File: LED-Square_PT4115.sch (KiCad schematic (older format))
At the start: 21 parts, among them P1 IN, P2 OUT, U1 PT4115-SOT89-5

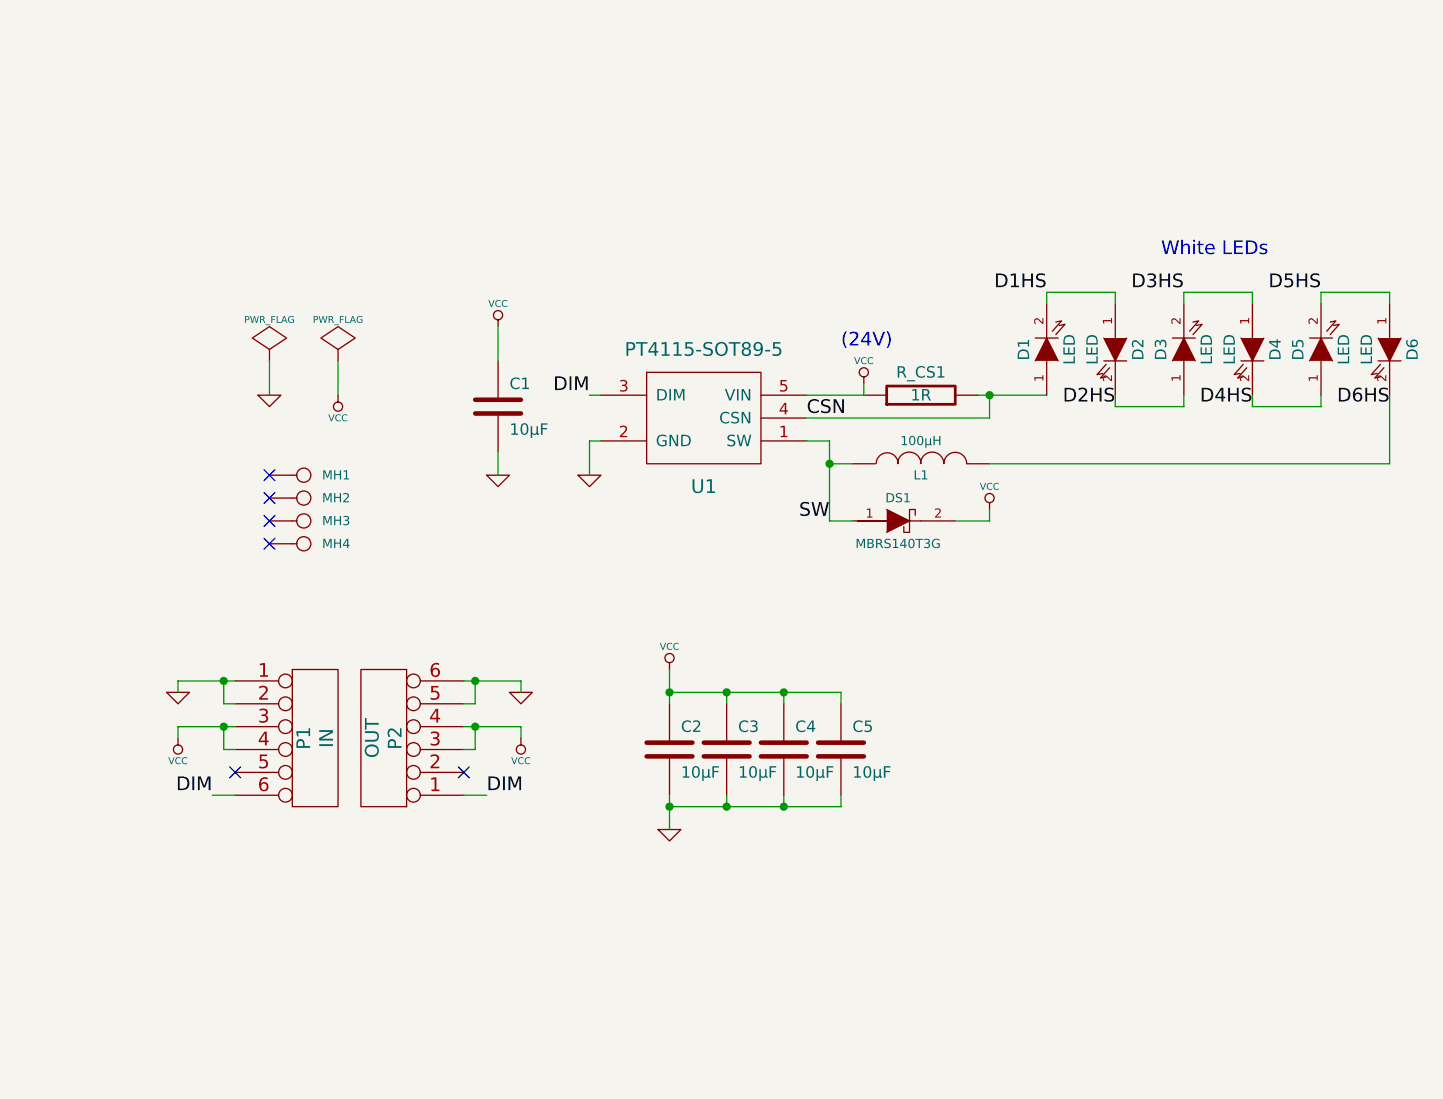
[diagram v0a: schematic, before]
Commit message: Added soft-start capacitor(s) - optional.
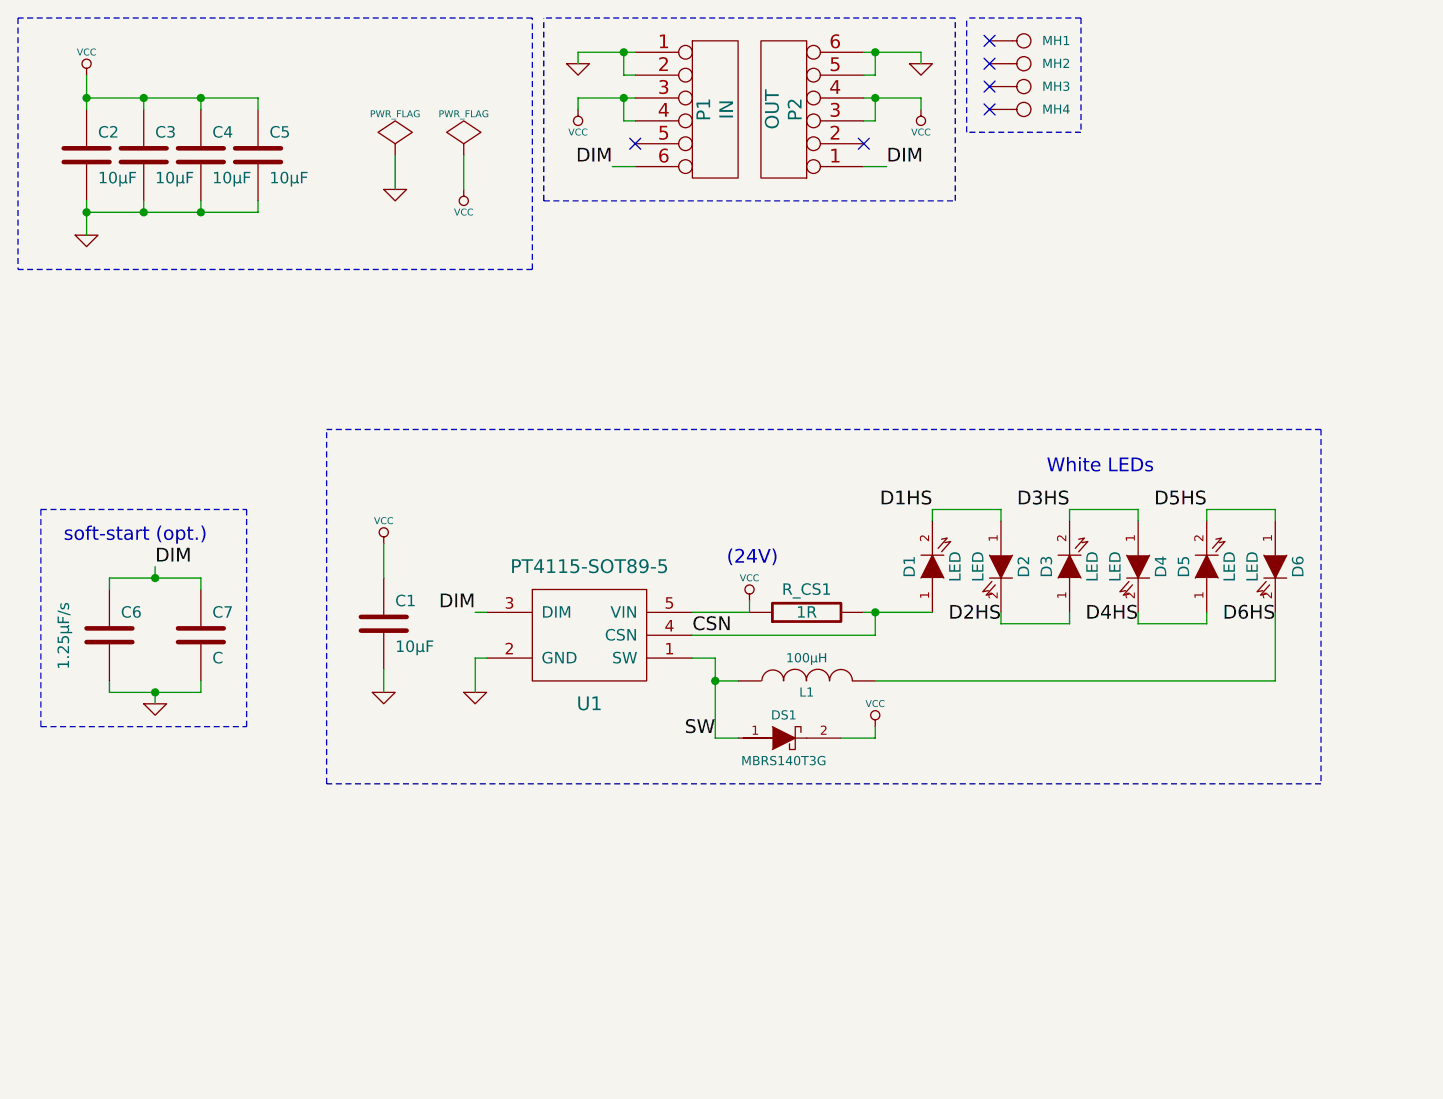
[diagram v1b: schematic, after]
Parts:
- added C6: 1.25µF/s, symbol C
- added C7: C, symbol C
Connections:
- net DIM: now also C6.1, C7.1
- net GND: now also C6.2, C7.2
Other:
- note added: "soft-start (opt.)"
- moved on the sheet: C1, C2, C3, C4, C5, D1, D2, D3, D4, D5, D6, DS1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

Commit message: Soft-start: replaced C7 with R1 (1M bleed resistor) for remaining C6.
R1 is not strictly necessary, but it speeds up discharging C6 a lot.
Without R1 it takes some time, maybe minutes, until soft-start
works again.
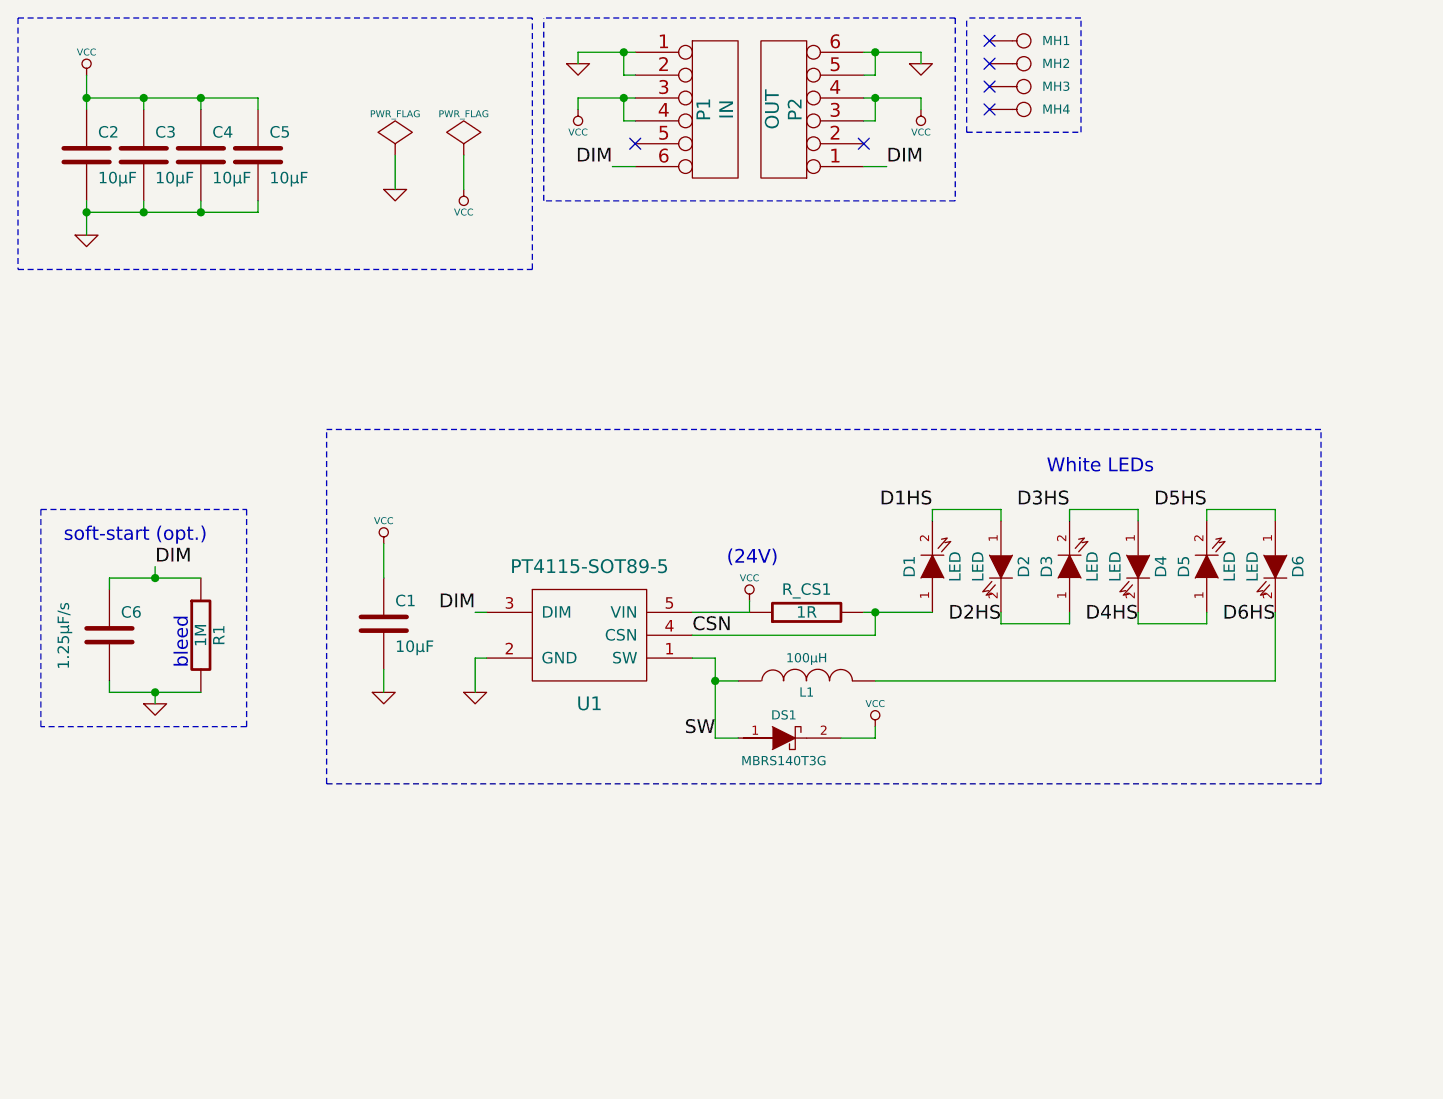
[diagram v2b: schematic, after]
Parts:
- removed C7: C, symbol C
- added R1: 1M, symbol R
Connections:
- net DIM: now also R1.1
- net GND: now also R1.2
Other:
- note added: "bleed"
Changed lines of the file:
@@
-EESchema Schematic File Version 2  date Sat 27 Oct 2012 06:55:14 PM CEST
+EESchema Schematic File Version 2  date Sun 11 Nov 2012 12:08:53 AM CET
 LIBS:my_parts
 LIBS:power
@@
 Sheet 1 1
 Title "LED-Square PT4115"
-Date "27 oct 2012"
+Date "10 nov 2012"
 Rev "0.10"
 Comp "2012 - blog.spitzenpfeil.org"
@@
 Comment4 ""
 $EndDescr
+Text Notes 1300 3400 1    60   ~ 0
+bleed
+Connection ~ 1150 3000
+Wire Wire Line
+	1150 2950 1150 3000
+Wire Wire Line
+	1350 3500 950  3500
+Wire Wire Line
+	1350 3000 950  3000
+Wire Notes Line
+	1550 3650 1550 2700
+Wire Notes Line
+	1550 3650 650  3650
+Wire Notes Line
+	650  3650 650  2700
+Wire Notes Line
+	550  550  550  1650
+Wire Notes Line
+	4700 1050 4700 550
+Wire Notes Line
+	4700 1050 5200 1050
+Wire Notes Line
+	5200 1050 5200 550
+Wire Notes Line
+	5200 550  4700 550
+Wire Notes Line
+	4650 550  2850 550
+Wire Notes Line
+	4650 550  4650 1350
+Wire Notes Line
+	4650 1350 2850 1350
+Wire Notes Line
+	2850 1350 2850 550
+Connection ~ 850  900
+Wire Wire Line
+	850  800  850  950
+Connection ~ 1100 1400
+Wire Wire Line
+	1100 1350 1100 1400
+Wire Wire Line
+	1600 1350 1600 1400
+Wire Wire Line
+	1600 1400 850  1400
+Connection ~ 1350 900
+Wire Wire Line
+	1350 950  1350 900
+Connection ~ 4300 700
+Wire Wire Line
+	4300 700  4300 800
+Wire Wire Line
+	4300 800  4250 800
+Connection ~ 4300 900
+Wire Wire Line
+	4300 900  4300 1000
+Wire Wire Line
+	4300 1000 4250 1000
+Wire Wire Line
+	4250 1200 4350 1200
+Wire Wire Line
+	3150 1200 3250 1200
+Wire Wire Line
+	3250 1000 3200 1000
+Connection ~ 3200 900
+Wire Wire Line
+	3200 1000 3200 900
+Connection ~ 3200 700
+Wire Wire Line
+	3200 700  3200 800
+Wire Wire Line
+	3200 800  3250 800
+Wire Wire Line
+	2500 1150 2500 1300
+Connection ~ 3600 3450
+Wire Wire Line
+	3700 3700 3600 3700
+Wire Wire Line
+	3600 3700 3600 3350
+Wire Wire Line
+	6050 3150 6050 3450
+Wire Wire Line
+	6050 3450 4300 3450
+Connection ~ 4300 3150
+Wire Wire Line
+	4550 3150 4250 3150
+Wire Wire Line
+	2150 2850 2150 3000
+Wire Wire Line
+	3750 3100 3750 3150
+Wire Wire Line
+	3750 3150 3500 3150
+Wire Wire Line
+	6050 2750 6050 2700
+Wire Wire Line
+	6050 2700 5750 2700
+Wire Wire Line
+	5750 2700 5750 2750
+Wire Wire Line
+	5450 2750 5450 2700
+Wire Wire Line
+	5450 2700 5150 2700
+Wire Wire Line
+	5150 2700 5150 2750
+Wire Wire Line
+	4850 2750 4850 2700
+Wire Wire Line
+	4850 2700 4550 2700
+Wire Wire Line
+	4550 2700 4550 2750
+Wire Wire Line
+	4850 3150 4850 3200
+Wire Wire Line
+	4850 3200 5150 3200
+Wire Wire Line
+	5150 3200 5150 3150
+Wire Wire Line
+	5450 3150 5450 3200
+Wire Wire Line
+	5450 3200 5750 3200
+Wire Wire Line
+	5750 3200 5750 3150
+Wire Wire Line
+	2600 3350 2550 3350
+Wire Wire Line
+	2550 3350 2550 3500
+Wire Wire Line
+	3500 3250 4300 3250
+Wire Wire Line
+	4300 3250 4300 3150
+Wire Wire Line
+	2150 3400 2150 3500
+Wire Wire Line
+	3600 3350 3500 3350
+Wire Wire Line
+	3600 3450 3700 3450
+Wire Wire Line
+	4150 3700 4300 3700
+Wire Wire Line
+	4300 3700 4300 3650
+Wire Wire Line
+	2200 1150 2200 1300
+Wire Wire Line
+	3000 750  3000 700
+Wire Wire Line
+	3000 700  3250 700
+Wire Wire Line
+	3000 950  3000 900
+Wire Wire Line
+	3000 900  3250 900
+Wire Wire Line
+	2550 3150 2600 3150
+Wire Wire Line
+	4250 900  4500 900
+Wire Wire Line
+	4500 900  4500 950
+Wire Wire Line
+	4250 700  4500 700
+Wire Wire Line
+	4500 700  4500 750
+Wire Wire Line
+	850  900  1600 900
+Wire Wire Line
+	1600 900  1600 950
+Wire Wire Line
+	1100 950  1100 900
+Connection ~ 1100 900
+Wire Wire Line
+	1350 1350 1350 1400
+Connection ~ 1350 1400
+Wire Wire Line
+	850  1500 850  1350
+Connection ~ 850  1400
+Wire Notes Line
+	550  550  2800 550
+Wire Notes Line
+	550  1650 2800 1650
+Wire Notes Line
+	2800 1650 2800 550
+Wire Notes Line
+	1900 3900 1900 2350
+Wire Notes Line
+	1900 3900 6250 3900
+Wire Notes Line
+	6250 3900 6250 2350
+Wire Notes Line
+	6250 2350 1900 2350
+Wire Wire Line
+	950  3000 950  3050
+Wire Wire Line
+	950  3500 950  3450
 Wire Notes Line
 	650  2700 1550 2700
 Wire Wire Line
-	1150 3500 1150 3550
-Connection ~ 1150 3000
-Wire Wire Line
-	1350 3450 1350 3500
-Wire Wire Line
-	1350 3500 950  3500
-Wire Wire Line
-	950  3500 950  3450
-Wire Wire Line
-	950  3050 950  3000
-Wire Notes Line
-	6250 2350 1900 2350
-Wire Notes Line
-	6250 2350 6250 3900
-Wire Notes Line
-	6250 3900 1900 3900
-Wire Notes Line
-	1900 3900 1900 2350
-Wire Notes Line
-	2800 1650 2800 550
-Wire Notes Line
-	2800 1650 550  1650
-Wire Notes Line
-	2800 550  550  550
-Connection ~ 850  1400
-Wire Wire Line
-	850  1500 850  1350
-Connection ~ 1350 1400
-Wire Wire Line
-	1350 1350 1350 1400
-Connection ~ 1100 900
-Wire Wire Line
-	1100 950  1100 900
-Wire Wire Line
-	1600 950  1600 900
-Wire Wire Line
-	1600 900  850  900
-Wire Wire Line
-	4500 750  4500 700
-Wire Wire Line
-	4500 700  4250 700
-Wire Wire Line
-	4500 950  4500 900
-Wire Wire Line
-	4500 900  4250 900
-Wire Wire Line
-	2550 3150 2600 3150
-Wire Wire Line
-	3250 900  3000 900
-Wire Wire Line
-	3000 900  3000 950
-Wire Wire Line
-	3250 700  3000 700
-Wire Wire Line
-	3000 700  3000 750
-Wire Wire Line
-	2200 1150 2200 1300
-Wire Wire Line
-	4300 3650 4300 3700
-Wire Wire Line
-	4300 3700 4150 3700
-Wire Wire Line
-	3600 3450 3700 3450
-Wire Wire Line
-	3500 3350 3600 3350
-Wire Wire Line
-	2150 3400 2150 3500
-Wire Wire Line
-	4300 3150 4300 3250
-Wire Wire Line
-	4300 3250 3500 3250
-Wire Wire Line
-	2550 3500 2550 3350
-Wire Wire Line
-	2550 3350 2600 3350
-Wire Wire Line
-	5750 3150 5750 3200
-Wire Wire Line
-	5750 3200 5450 3200
-Wire Wire Line
-	5450 3200 5450 3150
-Wire Wire Line
-	5150 3150 5150 3200
-Wire Wire Line
-	5150 3200 4850 3200
-Wire Wire Line
-	4850 3200 4850 3150
-Wire Wire Line
-	4550 2750 4550 2700
-Wire Wire Line
-	4550 2700 4850 2700
-Wire Wire Line
-	4850 2700 4850 2750
-Wire Wire Line
-	5150 2750 5150 2700
-Wire Wire Line
-	5150 2700 5450 2700
-Wire Wire Line
-	5450 2700 5450 2750
-Wire Wire Line
-	5750 2750 5750 2700
-Wire Wire Line
-	5750 2700 6050 2700
-Wire Wire Line
-	6050 2700 6050 2750
-Wire Wire Line
-	3500 3150 3750 3150
-Wire Wire Line
-	3750 3150 3750 3100
-Wire Wire Line
-	2150 2850 2150 3000
-Wire Wire Line
-	4550 3150 4250 3150
-Connection ~ 4300 3150
-Wire Wire Line
-	4300 3450 6050 3450
-Wire Wire Line
-	6050 3450 6050 3150
-Wire Wire Line
-	3600 3350 3600 3700
-Wire Wire Line
-	3600 3700 3700 3700
-Connection ~ 3600 3450
-Wire Wire Line
-	2500 1150 2500 1300
-Wire Wire Line
-	3250 800  3200 800
-Wire Wire Line
-	3200 800  3200 700
-Connection ~ 3200 700
-Wire Wire Line
-	3200 900  3200 1000
-Connection ~ 3200 900
-Wire Wire Line
-	3200 1000 3250 1000
-Wire Wire Line
-	3150 1200 3250 1200
-Wire Wire Line
-	4250 1200 4350 1200
-Wire Wire Line
-	4250 1000 4300 1000
-Wire Wire Line
-	4300 1000 4300 900
-Connection ~ 4300 900
-Wire Wire Line
-	4250 800  4300 800
-Wire Wire Line
-	4300 800  4300 700
-Connection ~ 4300 700
-Wire Wire Line
-	1350 950  1350 900
-Connection ~ 1350 900
-Wire Wire Line
-	850  1400 1600 1400
-Wire Wire Line
-	1600 1400 1600 1350
-Wire Wire Line
-	1100 1350 1100 1400
-Connection ~ 1100 1400
-Wire Wire Line
-	850  800  850  950
-Connection ~ 850  900
-Wire Notes Line
-	2850 1350 2850 550
-Wire Notes Line
-	2850 1350 4650 1350
-Wire Notes Line
-	4650 1350 4650 550
-Wire Notes Line
-	4650 550  2850 550
-Wire Notes Line
-	5200 550  4700 550
-Wire Notes Line
-	5200 550  5200 1050
-Wire Notes Line
-	5200 1050 4700 1050
-Wire Notes Line
-	4700 1050 4700 550
-Wire Notes Line
-	550  550  550  1650
-Wire Wire Line
-	950  3000 1350 3000
-Wire Wire Line
-	1350 3000 1350 3050
+	1150 3550 1150 3500
 Connection ~ 1150 3500
-Wire Wire Line
-	1150 2950 1150 3000
-Wire Notes Line
-	650  2700 650  3650
-Wire Notes Line
-	650  3650 1550 3650
-Wire Notes Line
-	1550 3650 1550 2700
 $Comp
-L C C7
-U 1 1 508C055B
+L R R1
+U 1 1 509EDDE6
 P 1350 3250
-F 0 "C7" H 1400 3350 50  0000 L CNN
-F 1 "C" H 1400 3150 50  0000 L CNN
+F 0 "R1" V 1430 3250 50  0000 C CNN
+F 1 "1M" V 1350 3250 50  0000 C CNN
 	1    1350 3250
 	1    0    0    -1
